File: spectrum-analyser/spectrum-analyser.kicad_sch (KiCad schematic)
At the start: 29 parts, among them J1 Conn_Coaxial, Q1 PMOS, Q2 PMOS, Q3 Q_PMOS_GSD, SW1 SW_SPDT, SW2 SW_UP, SW3 SW_RIGHT, SW4 SW_LEFT, SW5 SW_DOWN, U1 1.3" OLED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

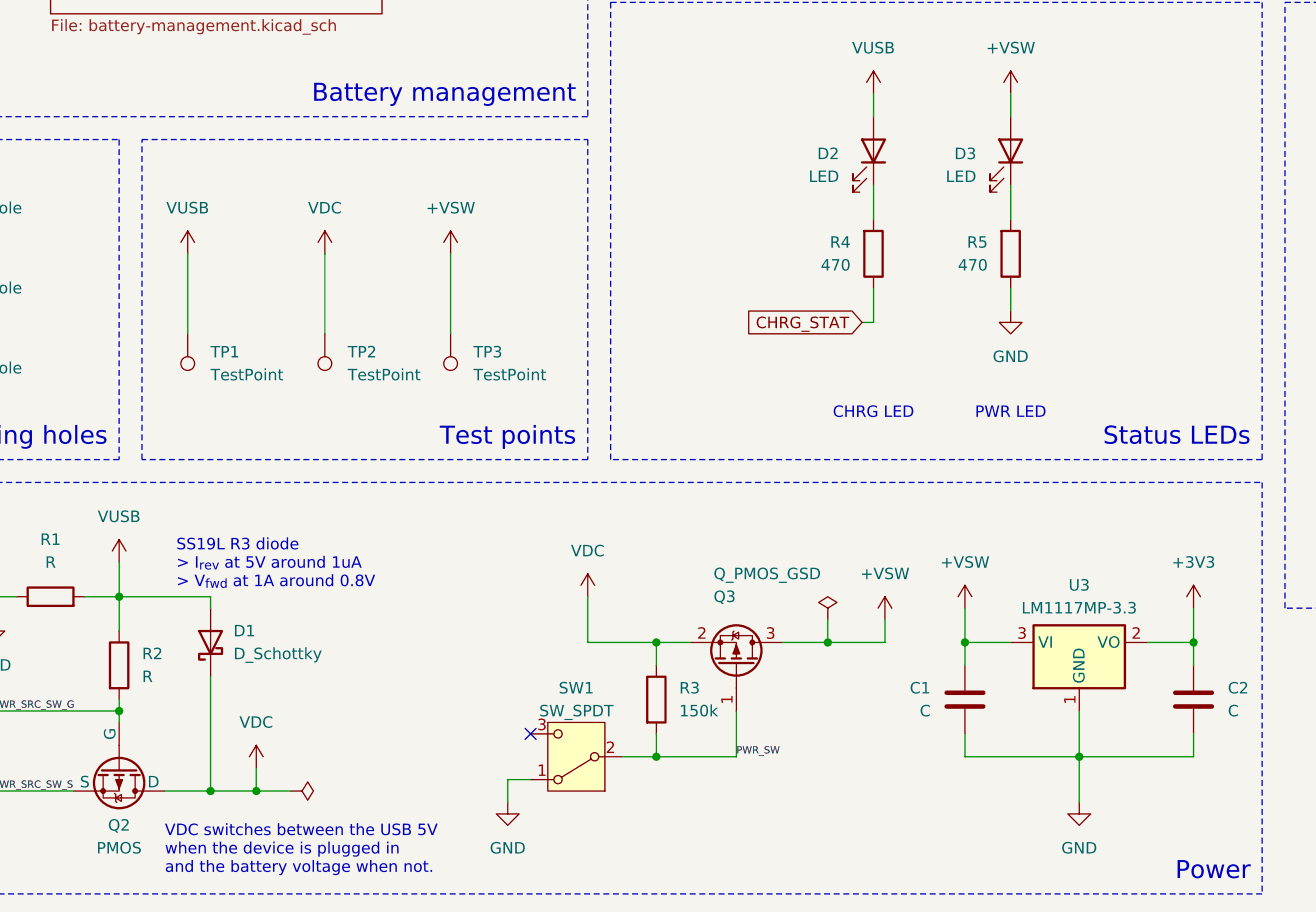
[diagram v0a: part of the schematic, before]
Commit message: Add informational silkscreen and change 3v3 LDO package
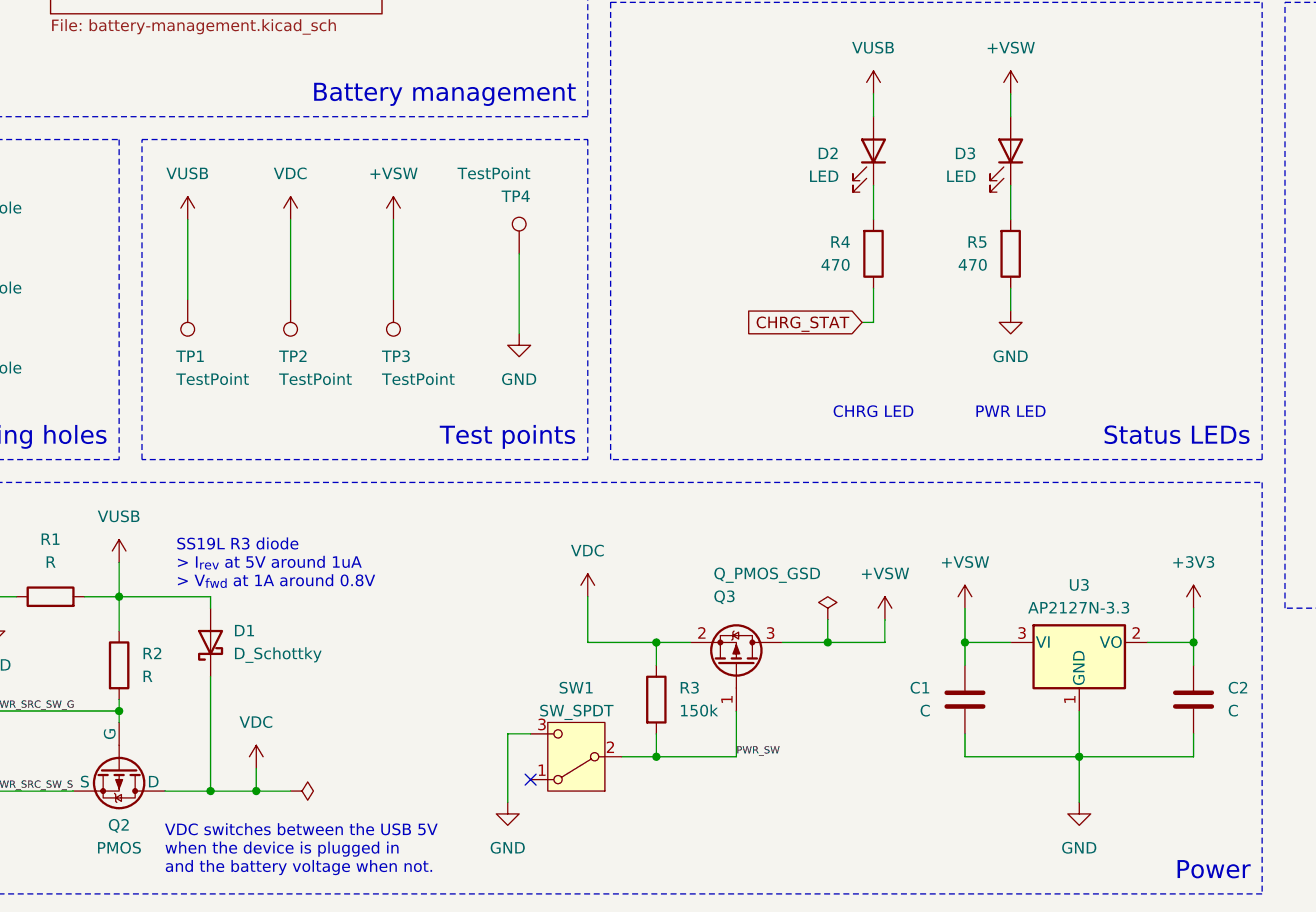
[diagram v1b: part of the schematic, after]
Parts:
- removed U3: LM1117MP-3.3, Package_TO_SOT_SMD:SOT-223-3_TabPin2, symbol Regulator_Linear:LM1117MP-3.3
- added TP4: TestPoint, TestPoint:TestPoint_THTPad_D2.0mm_Drill1.0mm, symbol Connector:TestPoint
- added U3: AP2127N-3.3, Package_TO_SOT_SMD:SOT-23, symbol Regulator_Linear:AP2127N-3.3
- H1, H2, H3: footprint MountingHole:MountingHole_2.7mm_M2.5 -> MountingHole:MountingHole_3.2mm_M3_ISO7380
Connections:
- net +3V3: now also U3.2 (VO)
- net +VSW: now also U3.3 (VI)
- net GND: now also SW1.3 (C), TP4.1, U3.1 (GND); no longer SW1.1 (A)
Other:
- moved on the sheet: TP1, TP2, TP3

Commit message: Assign component values and add charger capacitors
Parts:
- C1, C2: value C -> 1u
- J1: value Conn_Coaxial -> SMA
- Q1, Q2: value PMOS -> Q_PMOS_GSD; symbol Simulation_SPICE:PMOS -> Device:Q_PMOS_GSD
- R1, R2: value R -> 10k
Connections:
- net +BATT: now also Q1.3 (D); no longer Q1.1 (D)
- net PWR_SRC_SW_G: now also Q1.1 (G), Q2.1 (G); no longer Q1.2 (G), Q2.2 (G)
- net PWR_SRC_SW_S: now also Q1.2 (S), Q2.2 (S); no longer Q1.3 (S), Q2.3 (S)
- net VDC: now also Q2.3 (D); no longer Q2.1 (D)
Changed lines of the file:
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@@
 			)
 		)
-		(property "Value" "Conn_Coaxial"
+		(property "Value" "SMA"
 			(at 254 127.2931 0)
 			(effects
@@
 	)
 	(symbol
-		(lib_id "Simulation_SPICE:PMOS")
+		(lib_id "Device:Q_PMOS_GSD")
 		(at 26.67 180.34 90)
 		(mirror x)
@@
 			)
 		)
-		(property "Value" "PMOS"
+		(property "Value" "Q_PMOS_GSD"
 			(at 26.67 189.23 90)
 			(effects
@@
 			)
 		)
-		(property "Datasheet" "https://ngspice.sourceforge.io/docs/ngspice-html-manual/manual.xhtml#cha_MOSFETs"
-			(at 39.37 180.34 0)
-			(effects
-				(font
-					(size 1.27 1.27)
-				)
-				(hide yes)
-			)
-		)
-		(property "Description" "P-MOSFET transistor, drain/source/gate"
+		(property "Datasheet" "~"
+			(at 26.67 180.34 0)
+			(effects
+				(font
+					(size 1.27 1.27)
+				)
+				(hide yes)
+			)
+		)
+		(property "Description" "P-MOSFET transistor, gate/source/drain"
 			(at 26.67 180.34 0)
 			(effects
@@
 	)
 	(symbol
-		(lib_id "Simulation_SPICE:PMOS")
+		(lib_id "Device:Q_PMOS_GSD")
 		(at 46.99 180.34 270)
 		(unit 1)
@@
 			)
 		)
-		(property "Value" "PMOS"
+		(property "Value" "Q_PMOS_GSD"
 			(at 46.99 189.23 90)
 			(effects
@@
 			)
 		)
-		(property "Datasheet" "https://ngspice.sourceforge.io/docs/ngspice-html-manual/manual.xhtml#cha_MOSFETs"
-			(at 34.29 180.34 0)
-			(effects
-				(font
-					(size 1.27 1.27)
-				)
-				(hide yes)
-			)
-		)
-		(property "Description" "P-MOSFET transistor, drain/source/gate"
+		(property "Datasheet" "~"
+			(at 46.99 180.34 0)
+			(effects
+				(font
+					(size 1.27 1.27)
+				)
+				(hide yes)
+			)
+		)
+		(property "Description" "P-MOSFET transistor, gate/source/drain"
 			(at 46.99 180.34 0)
 			(effects
@@
 			)
 		)
-		(property "Value" "C"
+		(property "Value" "1u"
 			(at 170.18 173.9899 0)
 			(effects
@@
 			)
 		)
-		(property "Value" "C"
+		(property "Value" "1u"
 			(at 137.16 173.9899 0)
 			(effects
@@
 			)
 		)
-		(property "Value" "R"
+		(property "Value" "10k"
 			(at 49.53 170.1799 0)
 			(effects
@@
 			)
 		)
-		(property "Value" "R"
+		(property "Value" "10k"
 			(at 39.37 157.48 90)
 			(effects

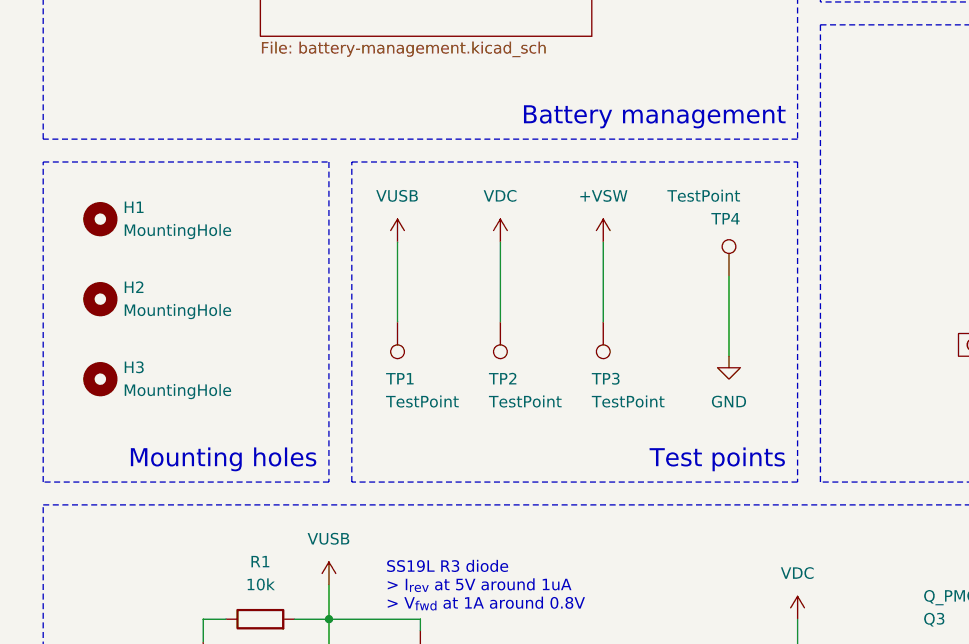
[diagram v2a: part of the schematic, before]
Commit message: Add Batt+ test point
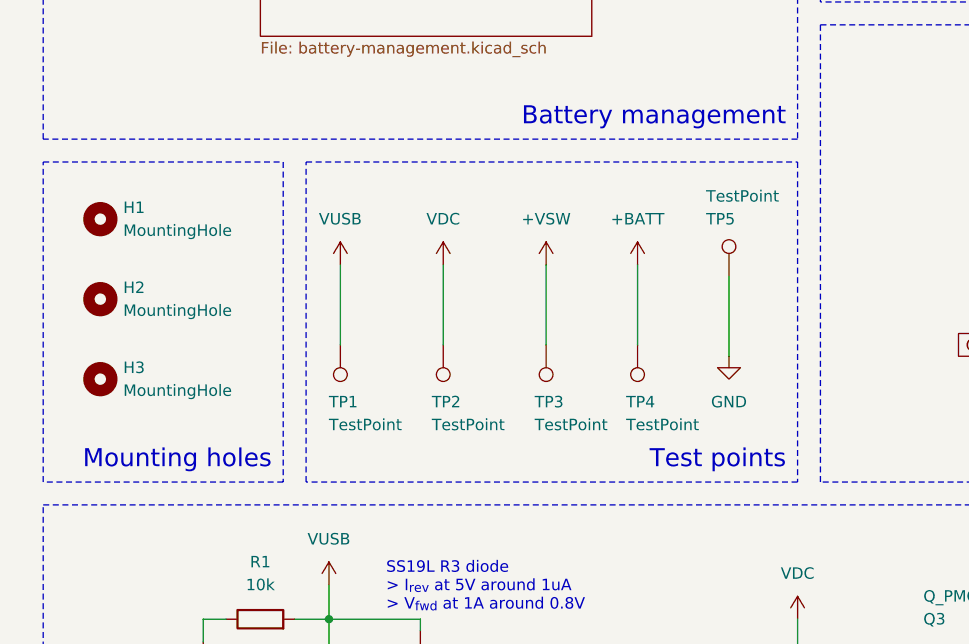
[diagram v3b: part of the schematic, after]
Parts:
- added TP4: TestPoint, TestPoint:TestPoint_Pad_D2.0mm, symbol Connector:TestPoint
- renumbered TP4 to TP5
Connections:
- net +BATT: now also TP4.1
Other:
- moved on the sheet: TP1, TP2, TP3
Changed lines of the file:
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@@
 	(wire
 		(pts
-			(xy 54.61 119.38) (xy 54.61 128.27)
+			(xy 48.26 121.92) (xy 48.26 130.81)
 		)
 		(stroke
@@
 	(wire
 		(pts
-			(xy 66.04 119.38) (xy 66.04 128.27)
+			(xy 59.69 121.92) (xy 59.69 130.81)
 		)
 		(stroke
@@
 	(wire
 		(pts
-			(xy 77.47 119.38) (xy 77.47 128.27)
+			(xy 71.12 121.92) (xy 71.12 130.81)
 		)
 		(stroke
@@
 	(wire
 		(pts
+			(xy 81.28 121.92) (xy 81.28 130.81)
+		)
+		(stroke
+			(width 0)
+			(type default)
+		)
+	)
+	(wire
+		(pts
 			(xy 57.15 162.56) (xy 57.15 161.29)
 		)
@@
 	)
 	(rectangle
-		(start 49.53 110.49)
+		(start 44.45 110.49)
 		(end 99.06 146.05)
 		(stroke
@@
 	(rectangle
 		(start 15.24 110.49)
-		(end 46.99 146.05)
+		(end 41.91 146.05)
 		(stroke
 			(width 0)
@@
 	(text "Mounting holes"
 		(exclude_from_sim no)
-		(at 45.72 144.78 0)
+		(at 40.64 144.78 0)
 		(effects
 			(font
@@
 	)
 	(symbol
+		(lib_id "Connector:TestPoint")
+		(at 81.28 130.81 180)
+		(unit 1)
+		(exclude_from_sim no)
+		(in_bom yes)
+		(on_board yes)
+		(dnp no)
+		(property "Reference" "TP4"
+			(at 80.01 137.16 0)
+			(effects
+				(font
+					(size 1.27 1.27)
+				)
+				(justify right)
+			)
+		)
+		(property "Value" "TestPoint"
+			(at 80.01 139.7 0)
+			(effects
+				(font
+					(size 1.27 1.27)
+				)
+				(justify right)
+			)
+		)
+		(property "Footprint" "TestPoint:TestPoint_Pad_D2.0mm"
+			(at 76.2 130.81 0)
+			(effects
+				(font
+					(size 1.27 1.27)
+				)
+				(hide yes)
+			)
+		)
+		(property "Datasheet" "~"
+			(at 76.2 130.81 0)
+			(effects
+				(font
+					(size 1.27 1.27)
+				)
+				(hide yes)
+			)
+		)
+		(property "Description" "test point"
+			(at 81.28 130.81 0)
+			(effects
+				(font
+					(size 1.27 1.27)
+				)
+				(hide yes)
+			)
+		)
+		(pin "1"
+		)
+		(instances
+			(project "spectrum-analyser"
+				(path "/e63e39d7-6ac0-4ffd-8aa3-1841a4541b55"
+					(reference "TP4")
+					(unit 1)
+				)
+			)
+		)
+	)
+	(symbol
 		(lib_id "Switch:SW_Push")
 		(at 254 40.64 0)
@@
 	(symbol
 		(lib_id "power:VDC")
-		(at 66.04 119.38 0)
+		(at 59.69 121.92 0)
 		(mirror y)
 		(unit 1)
@@
 		(dnp no)
 		(property "Reference" "#PWR04"
-			(at 66.04 121.92 0)
+			(at 59.69 124.46 0)
 			(effects
 				(font
@@
 		)
 		(property "Value" "VDC"
-			(at 66.04 114.3 0)
+			(at 59.69 116.84 0)
 			(effects
 				(font
@@
 		)
 		(property "Footprint" ""
-			(at 66.04 119.38 0)
+			(at 59.69 121.92 0)
 			(effects
 				(font
@@
 		)
 		(property "Datasheet" ""
-			(at 66.04 119.38 0)
+			(at 59.69 121.92 0)
 			(effects
 				(font
@@
 		)
 		(property "Description" ""
-			(at 66.04 119.38 0)
+			(at 59.69 121.92 0)
 			(effects
 				(font
@@
 	(symbol
 		(lib_id "Connector:TestPoint")
-		(at 66.04 128.27 180)
+		(at 59.69 130.81 180)
 		(unit 1)
 		(exclude_from_sim no)
@@
 		(dnp no)
 		(property "Reference" "TP2"
-			(at 64.77 134.62 0)
+			(at 58.42 137.16 0)
 			(effects
 				(font
@@
 		)
 		(property "Value" "TestPoint"
-			(at 64.77 137.16 0)
+			(at 58.42 139.7 0)
 			(effects
 				(font
@@
 		)
 		(property "Footprint" "TestPoint:TestPoint_Pad_D2.0mm"
-			(at 60.96 128.27 0)
+			(at 54.61 130.81 0)
 			(effects
 				(font
@@
 		)
 		(property "Datasheet" "~"
-			(at 60.96 128.27 0)
+			(at 54.61 130.81 0)
 			(effects
 				(font
@@
 		)
 		(property "Description" "test point"
-			(at 66.04 128.27 0)
+			(at 59.69 130.81 0)
 			(effects
 				(font
@@
 	)
 	(symbol
+		(lib_id "power:+BATT")
+		(at 81.28 121.92 0)
+		(unit 1)
+		(exclude_from_sim no)
+		(in_bom yes)
+		(on_board yes)
+		(dnp no)
+		(fields_autoplaced yes)
+		(property "Reference" "#PWR040"
+			(at 81.28 125.73 0)
+			(effects
+				(font
+					(size 1.27 1.27)
+				)
+				(hide yes)
+			)
+		)
+		(property "Value" "+BATT"
+			(at 81.28 116.84 0)
+			(effects
+				(font
+					(size 1.27 1.27)
+				)
+			)
+		)
+		(property "Footprint" ""
+			(at 81.28 121.92 0)
+			(effects
+				(font
+					(size 1.27 1.27)
+				)
+				(hide yes)
+			)
+		)
+		(property "Datasheet" ""
+			(at 81.28 121.92 0)
+			(effects
+				(font
+					(size 1.27 1.27)
+				)
+				(hide yes)
+			)
+		)
+		(property "Description" "Power symbol creates a global label with name \"+BATT\""
+			(at 81.28 121.92 0)
+			(effects
+				(font
+					(size 1.27 1.27)
+				)
+				(hide yes)
+			)
+		)
+		(pin "1"
+		)
+		(instances
+			(project ""
+				(path "/e63e39d7-6ac0-4ffd-8aa3-1841a4541b55"
+					(reference "#PWR040")
+					(unit 1)
+				)
+			)
+		)
+	)
+	(symbol
 		(lib_id "power:GND")
 		(at 91.44 132.08 0)
@@
 	(symbol
 		(lib_id "Connector:TestPoint")
-		(at 54.61 128.27 180)
+		(at 48.26 130.81 180)
 		(unit 1)
 		(exclude_from_sim no)
@@
 		(dnp no)
 		(property "Reference" "TP1"
-			(at 53.34 134.62 0)
+			(at 46.99 137.16 0)
 			(effects
 				(font
@@
 		)
 		(property "Value" "TestPoint"
-			(at 53.34 137.16 0)
+			(at 46.99 139.7 0)
 			(effects
 				(font
@@
 		)
 		(property "Footprint" "TestPoint:TestPoint_Pad_D2.0mm"
-			(at 49.53 128.27 0)
+			(at 43.18 130.81 0)
 			(effects
 				(font
@@
 		)
 		(property "Datasheet" "~"
-			(at 49.53 128.27 0)
+			(at 43.18 130.81 0)
 			(effects
 				(font
@@
 		)
 		(property "Description" "test point"
-			(at 54.61 128.27 0)
+			(at 48.26 130.81 0)
 			(effects
 				(font
@@
 	(symbol
 		(lib_id "thanassis_sym:VUSB")
-		(at 54.61 119.38 0)
+		(at 48.26 121.92 0)
 		(unit 1)
 		(exclude_from_sim no)
@@
 		(fields_autoplaced yes)
 		(property "Reference" "#PWR02"
-			(at 54.61 123.19 0)
+			(at 48.26 125.73 0)
 			(effects
 				(font
@@
 		)
 		(property "Value" "VUSB"
-			(at 54.61 114.3 0)
+			(at 48.26 116.84 0)
 			(effects
 				(font
@@
 		)
 		(property "Footprint" ""
-			(at 54.61 119.38 0)
+			(at 48.26 121.92 0)
 			(effects
 				(font
@@
 		)
 		(property "Datasheet" ""
-			(at 54.61 119.38 0)
+			(at 48.26 121.92 0)
 			(effects
 				(font
@@
 		)
 		(property "Description" "Power symbol creates a global label with name \"VUSB\""
-			(at 54.61 119.38 0)
+			(at 48.26 121.92 0)
 			(effects
 				(font
@@
 		(lib_name "+VSW_1")
 		(lib_id "power:+VSW")
-		(at 77.47 119.38 0)
+		(at 71.12 121.92 0)
 		(unit 1)
 		(exclude_from_sim no)
@@
 		(fields_autoplaced yes)
 		(property "Reference" "#PWR08"
-			(at 77.47 123.19 0)
+			(at 71.12 125.73 0)
 			(effects
 				(font
@@
 		)
 		(property "Value" "+VSW"
-			(at 77.47 114.3 0)
+			(at 71.12 116.84 0)
 			(effects
 				(font
@@
 		)
 		(property "Footprint" ""
-			(at 77.47 119.38 0)
+			(at 71.12 121.92 0)
 			(effects
 				(font
@@
 		)
 		(property "Datasheet" ""
-			(at 77.47 119.38 0)
+			(at 71.12 121.92 0)
 			(effects
 				(font
@@
 		)
 		(property "Description" "Power symbol creates a global label with name \"+VSW\""
-			(at 77.47 119.38 0)
+			(at 71.12 121.92 0)
 			(effects
 				(font
@@
 		(on_board yes)
 		(dnp no)
-		(property "Reference" "TP4"
-			(at 92.71 116.84 0)
+		(property "Reference" "TP5"
+			(at 88.9 116.84 0)
 			(effects
 				(font
 					(size 1.27 1.27)
 				)
-				(justify right)
+				(justify left)
 			)
 		)
 		(property "Value" "TestPoint"
-			(at 92.71 114.3 0)
+			(at 88.9 114.3 0)
 			(effects
 				(font
 					(size 1.27 1.27)
 				)
-				(justify right)
+				(justify left)
 			)
 		)
@@
 			(project "spectrum-analyser"
 				(path "/e63e39d7-6ac0-4ffd-8aa3-1841a4541b55"
-					(reference "TP4")
+					(reference "TP5")
 					(unit 1)
 				)
@@
 	(symbol
 		(lib_id "Connector:TestPoint")
-		(at 77.47 128.27 180)
+		(at 71.12 130.81 180)
 		(unit 1)
 		(exclude_from_sim no)
@@
 		(dnp no)
 		(property "Reference" "TP3"
-			(at 76.2 134.62 0)
+			(at 69.85 137.16 0)
 			(effects
 				(font
@@
 		)
 		(property "Value" "TestPoint"
-			(at 76.2 137.16 0)
+			(at 69.85 139.7 0)
 			(effects
 				(font
@@
 		)
 		(property "Footprint" "TestPoint:TestPoint_Pad_D2.0mm"
-			(at 72.39 128.27 0)
+			(at 66.04 130.81 0)
 			(effects
 				(font
@@
 		)
 		(property "Datasheet" "~"
-			(at 72.39 128.27 0)
+			(at 66.04 130.81 0)
 			(effects
 				(font
@@
 		)
 		(property "Description" "test point"
-			(at 77.47 128.27 0)
+			(at 71.12 130.81 0)
 			(effects
 				(font
